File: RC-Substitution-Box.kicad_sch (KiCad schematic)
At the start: 59 parts, among them J13 Screw_Terminal_01x02, J14 Screw_Terminal_01x02, J5 Screw_Terminal_01x02, J6 Screw_Terminal_01x02, SW2 208-12, SW3 208-12, SW4 208-12, SW5 100SP3T1B1M2QE-ND, SW6 208-12, SW7 100SP3T1B1M2QE-ND

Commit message: PCB LAYOUT DONE
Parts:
- added H1, H2, H3, H4: MountingHole, MountingHole:MountingHole_3.2mm_M3_Pad, symbol Mechanical:MountingHole
- R22: footprint DJ-FOOTPRINTS:DIP SPST 12 Position -> DJ-FOOTPRINTS:RES-ADJ-TH_3P-L9.5-W9.5-P2.54-BR-BS
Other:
- moved on the sheet: R36

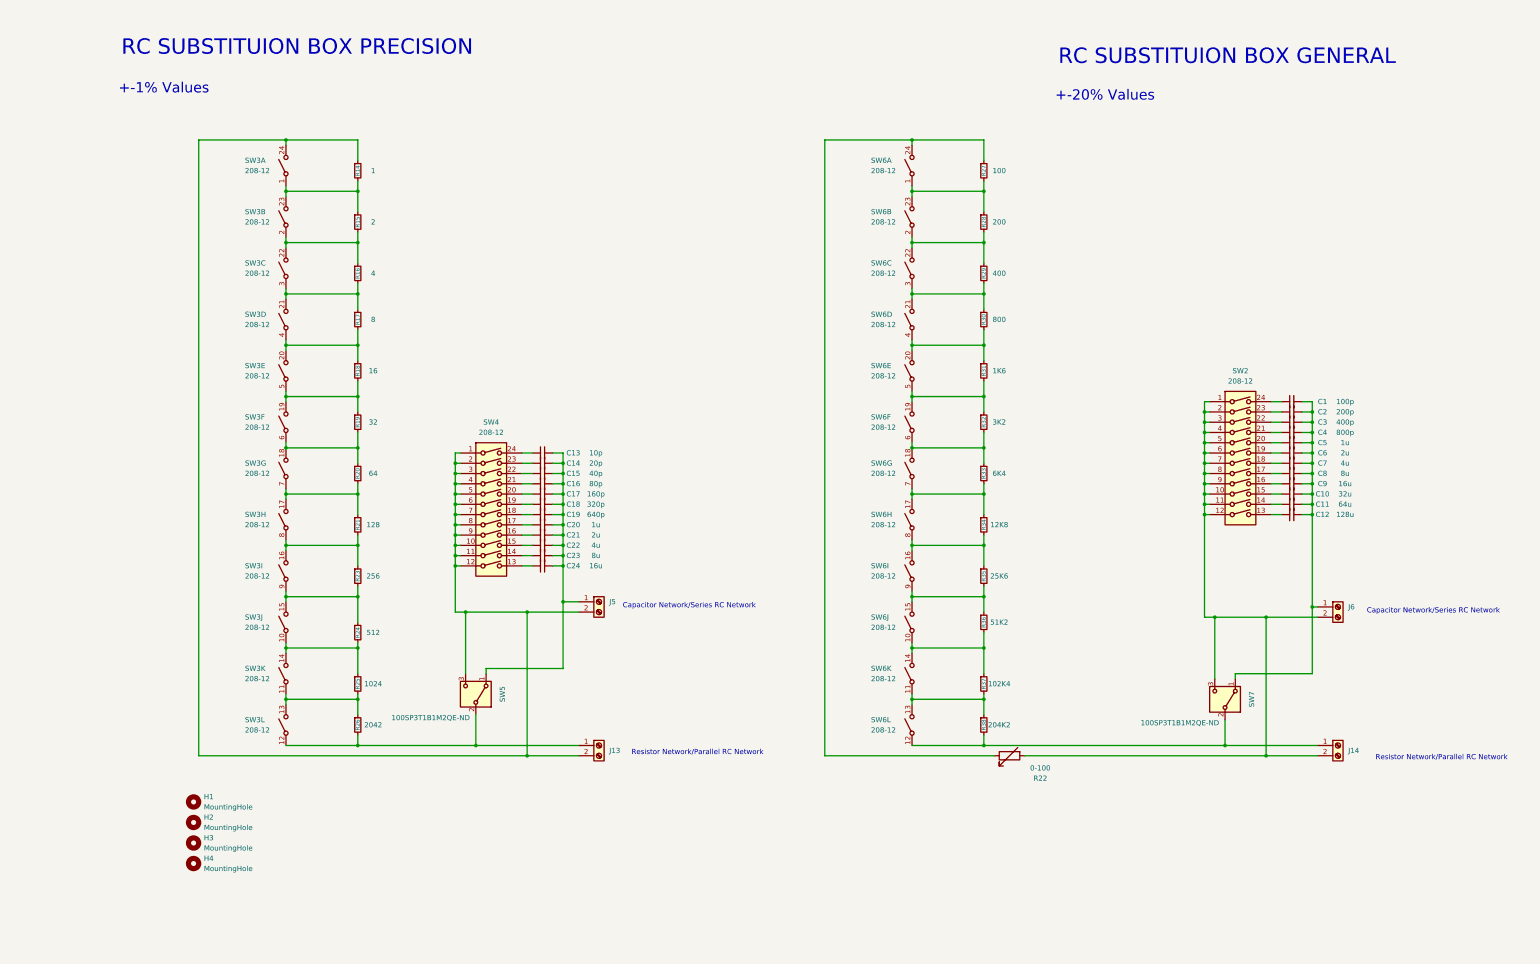
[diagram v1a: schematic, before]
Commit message: Removing SW and adding Axial RC Option
-Removing the SW becasue it is not needed
- Adding an axial option just for flexibility
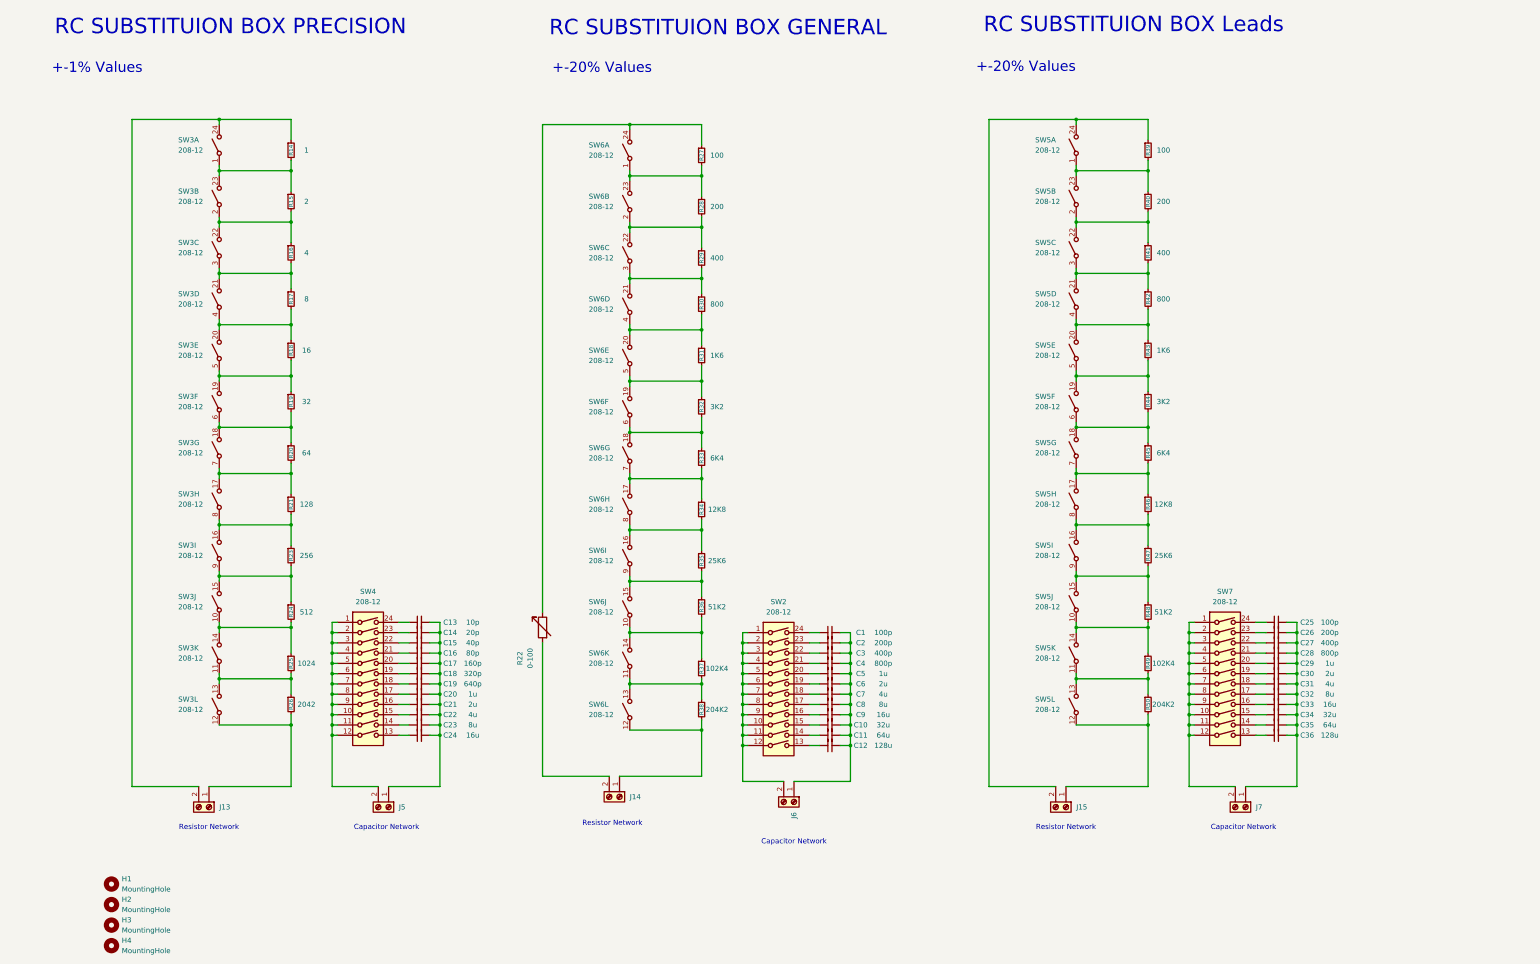
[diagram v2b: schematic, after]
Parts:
- removed SW5, SW7: 100SP3T1B1M2QE-ND, DJ-FOOTPRINTS:SW_100SP3T1B1M2QE, symbol Switch:SW_SPDT
- added C25: 100p, Capacitor_THT:C_Disc_D5.1mm_W3.2mm_P5.00mm, symbol Device:C_Small
- added C26: 200p, Capacitor_THT:C_Disc_D5.1mm_W3.2mm_P5.00mm, symbol Device:C_Small
- added C27: 400p, Capacitor_THT:C_Disc_D5.1mm_W3.2mm_P5.00mm, symbol Device:C_Small
- added C28: 800p, Capacitor_THT:C_Disc_D5.1mm_W3.2mm_P5.00mm, symbol Device:C_Small
- added C29: 1u, Capacitor_THT:C_Disc_D5.1mm_W3.2mm_P5.00mm, symbol Device:C_Small
- added C30: 2u, Capacitor_THT:C_Disc_D5.1mm_W3.2mm_P5.00mm, symbol Device:C_Small
- added C31: 4u, Capacitor_THT:C_Disc_D5.1mm_W3.2mm_P5.00mm, symbol Device:C_Small
- added C32: 8u, Capacitor_THT:C_Disc_D5.1mm_W3.2mm_P5.00mm, symbol Device:C_Small
- added C33: 16u, Capacitor_THT:C_Disc_D5.1mm_W3.2mm_P5.00mm, symbol Device:C_Small
- added C34: 32u, Capacitor_THT:C_Disc_D5.1mm_W3.2mm_P5.00mm, symbol Device:C_Small
- added C35: 64u, Capacitor_THT:C_Disc_D5.1mm_W3.2mm_P5.00mm, symbol Device:C_Small
- added C36: 128u, Capacitor_THT:C_Disc_D5.1mm_W3.2mm_P5.00mm, symbol Device:C_Small
- added J15, J7: Screw_Terminal_01x02, TerminalBlock_Phoenix:TerminalBlock_Phoenix_MKDS-1,5-2_1x02_P5.00mm_Horizontal, symbol Connector:Screw_Terminal_01x02
- added R39: 100, Resistor_THT:R_Axial_DIN0207_L6.3mm_D2.5mm_P7.62mm_Horizontal, symbol Device:R_Small
- added R40: 200, Resistor_THT:R_Axial_DIN0207_L6.3mm_D2.5mm_P7.62mm_Horizontal, symbol Device:R_Small
- added R41: 400, Resistor_THT:R_Axial_DIN0207_L6.3mm_D2.5mm_P7.62mm_Horizontal, symbol Device:R_Small
- added R42: 800, Resistor_THT:R_Axial_DIN0207_L6.3mm_D2.5mm_P7.62mm_Horizontal, symbol Device:R_Small
- added R43: 1K6, Resistor_THT:R_Axial_DIN0207_L6.3mm_D2.5mm_P7.62mm_Horizontal, symbol Device:R_Small
- added R44: 3K2, Resistor_THT:R_Axial_DIN0207_L6.3mm_D2.5mm_P7.62mm_Horizontal, symbol Device:R_Small
- added R45: 6K4, Resistor_THT:R_Axial_DIN0207_L6.3mm_D2.5mm_P7.62mm_Horizontal, symbol Device:R_Small
- added R46: 12K8, Resistor_THT:R_Axial_DIN0207_L6.3mm_D2.5mm_P7.62mm_Horizontal, symbol Device:R_Small
- added R47: 25K6, Resistor_THT:R_Axial_DIN0207_L6.3mm_D2.5mm_P7.62mm_Horizontal, symbol Device:R_Small
- added R48: 51K2, Resistor_THT:R_Axial_DIN0207_L6.3mm_D2.5mm_P7.62mm_Horizontal, symbol Device:R_Small
- added R49: 102K4, Resistor_THT:R_Axial_DIN0207_L6.3mm_D2.5mm_P7.62mm_Horizontal, symbol Device:R_Small
- added R50: 204K2, Resistor_THT:R_Axial_DIN0207_L6.3mm_D2.5mm_P7.62mm_Horizontal, symbol Device:R_Small
- added SW5: 208-12, Button_Switch_THT:SW_DIP_SPSTx12_Slide_9.78x32.66mm_W7.62mm_P2.54mm, symbol easyeda2kicad:SW_SPST_12
- added SW7: 208-12, Button_Switch_THT:SW_DIP_SPSTx12_Slide_9.78x32.66mm_W7.62mm_P2.54mm, symbol Switch:SW_DIP_x12
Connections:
- net at J6.2 (Pin_2), SW2.1, SW2.10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: no longer J14.2 (Pin_2), R22.2
- net at J5.2 (Pin_2), SW4.1, SW4.10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: no longer J13.2 (Pin_2), R14.1, SW3.24
- new net: R40.2, R41.1, SW5.2, SW5.22
- new net: R41.2, R42.1, SW5.21, SW5.3
- new net: C26.1, SW7.23
- new net: C25.2, C26.2, C27.2, C28.2, C29.2, C30.2, C31.2, C32.2, C33.2, C34.2, C35.2, C36.2, J7.1 (Pin_1)
- new net: J15.2 (Pin_2), R39.1, SW5.24
- new net: R39.2, R40.1, SW5.1, SW5.23
- new net: J14.2 (Pin_2), R22.2
- new net: R47.2, R48.1, SW5.15, SW5.9
- new net: R48.2, R49.1, SW5.10, SW5.14
- new net: R42.2, R43.1, SW5.20, SW5.4
- new net: R43.2, R44.1, SW5.19, SW5.5
- new net: R46.2, R47.1, SW5.16, SW5.8
- new net: R49.2, R50.1, SW5.11, SW5.13
- new net: J15.1 (Pin_1), R50.2, SW5.12
- new net: J13.2 (Pin_2), R14.1, SW3.24
- new net: C34.1, SW7.15
- new net: C29.1, SW7.20
- new net: C35.1, SW7.14
- new net: R44.2, R45.1, SW5.18, SW5.6
- new net: R45.2, R46.1, SW5.17, SW5.7
- new net: C30.1, SW7.19
- new net: C28.1, SW7.21
- new net: J7.2 (Pin_2), SW7.1, SW7.10, SW7.11, SW7.12, SW7.2, SW7.3, SW7.4, SW7.5, SW7.6, SW7.7, SW7.8, SW7.9
- new net: C36.1, SW7.13
- new net: C33.1, SW7.16
- new net: C32.1, SW7.17
- new net: C31.1, SW7.18
- new net: C27.1, SW7.22
- new net: C25.1, SW7.24
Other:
- note added: "Capacitor Network"
- note added: "RC SUBSTITUION BOX Leads"
- note added: "Resistor Network"
- note removed: "Capacitor Network/Series RC Network"
- note removed: "Resistor Network/Parallel RC Network"
- moved on the sheet: C1, C10, C11, C12, C13, C14, C15, C16, C17, C18, C19, C2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

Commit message: updated layout
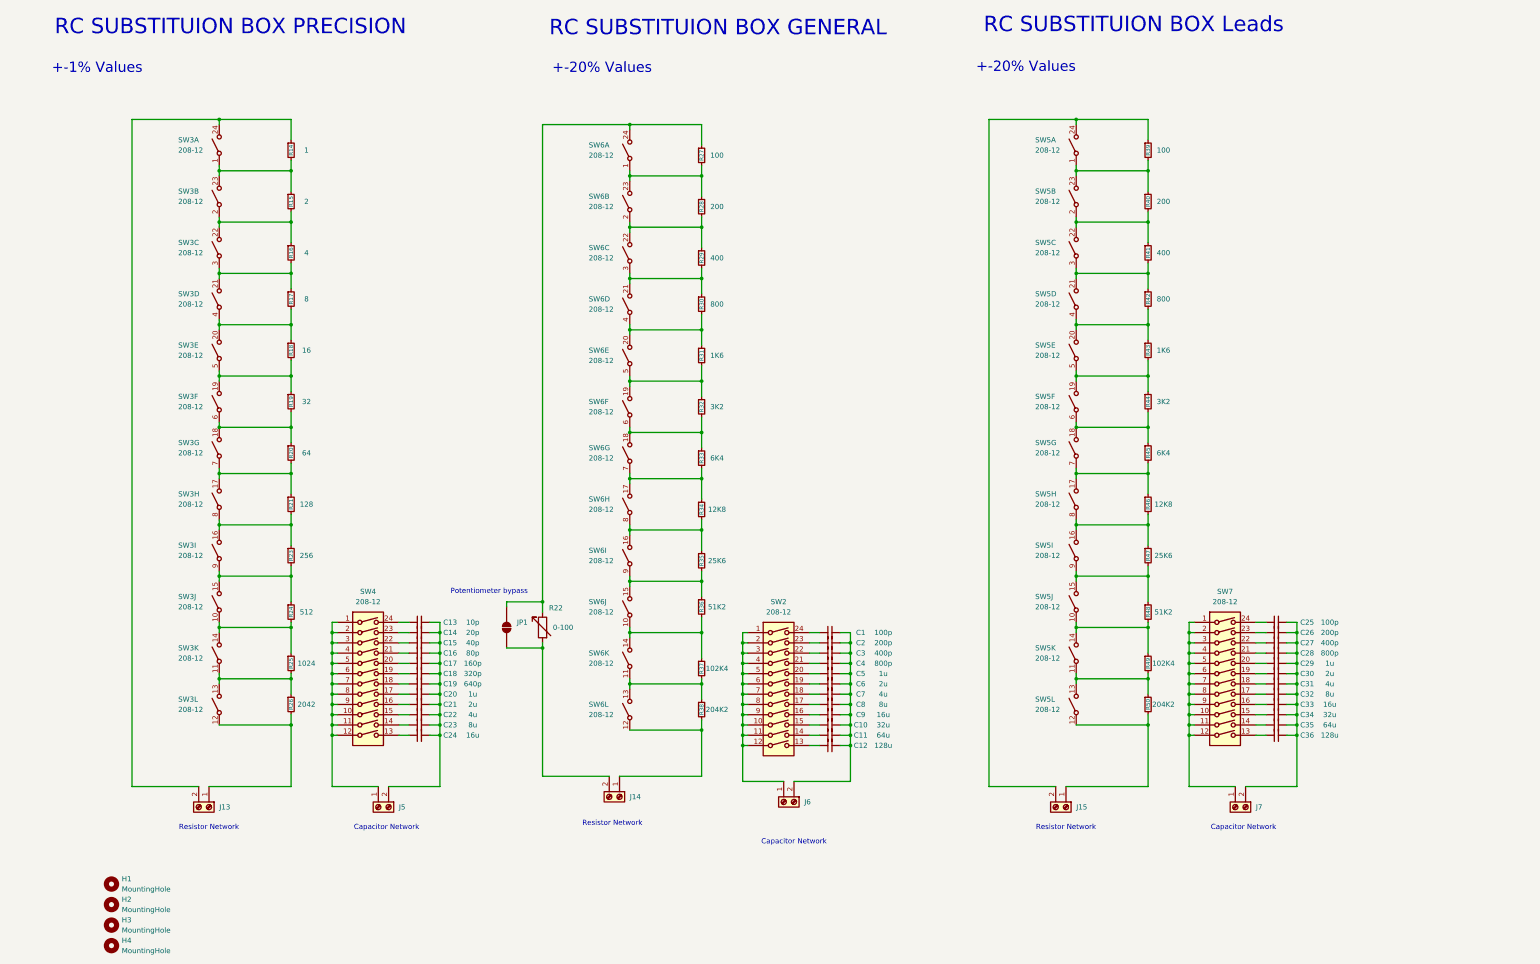
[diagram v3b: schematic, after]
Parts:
- added JP1: SolderJumper_2_Open, Jumper:SolderJumper-2_P1.3mm_Open_Pad1.0x1.5mm, symbol Jumper:SolderJumper_2_Open
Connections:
- net at C1.2, C10.2, C11.2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: now also J6.2 (Pin_2); no longer J6.1 (Pin_1)
- net at SW2.1, SW2.10, SW2.11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: now also J6.1 (Pin_1); no longer J6.2 (Pin_2)
- net at C25.2, C26.2, C27.2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: now also J7.2 (Pin_2); no longer J7.1 (Pin_1)
- net at J14.2 (Pin_2), R22.2: now also JP1.1 (A)
- net at C13.2, C14.2, C15.2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: now also J5.2 (Pin_2); no longer J5.1 (Pin_1)
- net at SW4.1, SW4.10, SW4.11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: now also J5.1 (Pin_1); no longer J5.2 (Pin_2)
- net at R22.1, R27.1, SW6.24: now also JP1.2 (B)
- net at SW7.1, SW7.10, SW7.11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: now also J7.1 (Pin_1); no longer J7.2 (Pin_2)
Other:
- note added: "Potentiometer bypass"
